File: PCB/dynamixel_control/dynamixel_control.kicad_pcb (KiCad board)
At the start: 4 copper layers, 36 x 56 mm, 56 parts, among them J1 12V, J11 Dynamixel TTL, J12 Dynamixel TTL, J2 RS232, J3 5V, J4 3.3V, J5 I2C, J8 Dynamixel TTL, Q1 SSM3J372R, Q2 IPD068P03L3GATMA1, Q3 T2N7002AK, SW1 LIMIT_SWITCH, U1 R-78E5.0-0.5, U2 SN74AHC1G14, U3 LM810M3-4.63, U4 Teensy_4.0, U5 MAX3221E, U6 ICM-40627, U7 SN74LV1T34, U8 SN74LVC2G241

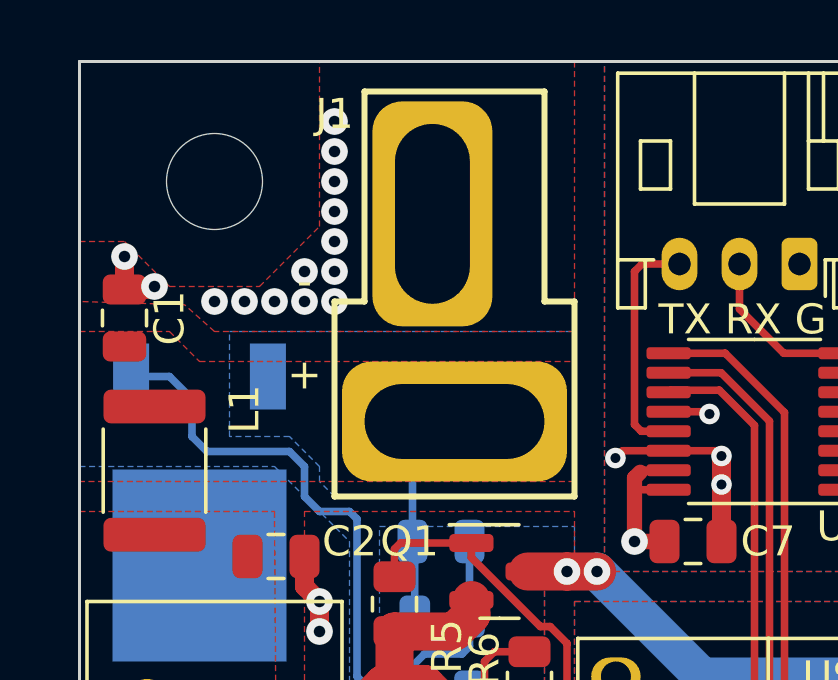
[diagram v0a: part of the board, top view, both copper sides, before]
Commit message: Fix T-Connector
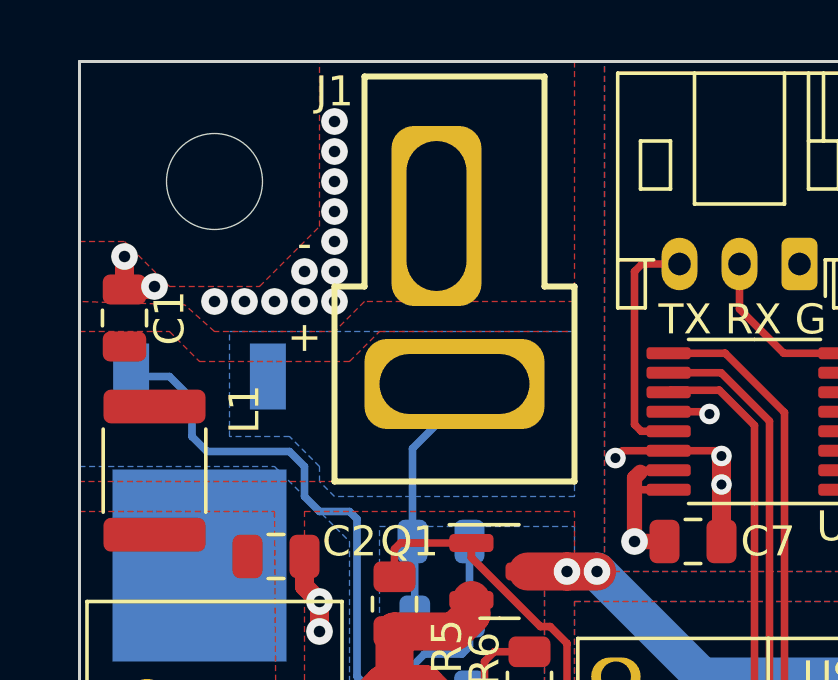
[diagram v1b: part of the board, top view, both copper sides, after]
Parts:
- moved J1 1.25 mm to (32.5, 30.8)
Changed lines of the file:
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@@
   )
   (footprint "t-top:t-connector" (layer "F.Cu")
-    (at 32.5 32 180)
+    (at 32.5 30.75 180)
     (property "Sheetfile" "dynamixel_control.kicad_sch")
     (property "Sheetname" "")
     (attr through_hole)
-    (fp_text reference "J1" (at 4 10.25 unlocked) (layer "F.SilkS")
+    (fp_text reference "J1" (at 4 9.75 unlocked) (layer "F.SilkS")
       (effects (font (size 1 1) (thickness 0.15)))
     )
@@
       (effects (font (size 1 1) (thickness 0.15)))
     )
-    (fp_line (start 3 11) (end 3 4) (layer "F.SilkS") (width 0.2))
-    (fp_line (start 3 4) (end 4 4) (layer "F.SilkS") (width 0.2))
-    (fp_line (start -3 11) (end 3 11) (layer "F.SilkS") (width 0.2))
-    (fp_line (start -4 4) (end -3 4) (layer "F.SilkS") (width 0.2))
-    (fp_line (start 4 -2.5) (end -4 -2.5) (layer "F.SilkS") (width 0.2))
-    (fp_line (start -3 4) (end -3 11) (layer "F.SilkS") (width 0.2))
-    (fp_line (start 4 4) (end 4 -2.5) (layer "F.SilkS") (width 0.2))
-    (fp_line (start -4 -2.5) (end -4 4) (layer "F.SilkS") (width 0.2))
-    (fp_line (start 4.5 -3) (end 4.5 11.5) (layer "F.CrtYd") (width 0.05))
-    (fp_line (start 4.5 11.5) (end -4.5 11.5) (layer "F.CrtYd") (width 0.05))
-    (fp_line (start -4.5 -3) (end 4.5 -3) (layer "F.CrtYd") (width 0.05))
-    (fp_line (start -4.5 11.5) (end -4.5 -3) (layer "F.CrtYd") (width 0.05))
-    (pad "1" thru_hole roundrect (at 0.7366 6.9215 180) (size 4 7.5) (drill oval 2.5 6) (layers *.Cu *.Mask) (roundrect_rratio 0.25)
+    (fp_line (start -4 -3.25) (end -4 3.25) (layer "F.SilkS") (width 0.2))
+    (fp_line (start 3 10.25) (end 3 3.25) (layer "F.SilkS") (width 0.2))
+    (fp_line (start 3 3.25) (end 4 3.25) (layer "F.SilkS") (width 0.2))
+    (fp_line (start -4 3.25) (end -3 3.25) (layer "F.SilkS") (width 0.2))
+    (fp_line (start -3 3.25) (end -3 10.25) (layer "F.SilkS") (width 0.2))
+    (fp_line (start -3 10.25) (end 3 10.25) (layer "F.SilkS") (width 0.2))
+    (fp_line (start 4 -3.25) (end -4 -3.25) (layer "F.SilkS") (width 0.2))
+    (fp_line (start 4 3.25) (end 4 -3.25) (layer "F.SilkS") (width 0.2))
+    (fp_line (start -4.5 10.75) (end -4.5 -3.75) (layer "F.CrtYd") (width 0.05))
+    (fp_line (start 4.5 -3.75) (end 4.5 10.75) (layer "F.CrtYd") (width 0.05))
+    (fp_line (start -4.5 -3.75) (end 4.5 -3.75) (layer "F.CrtYd") (width 0.05))
+    (fp_line (start 4.5 10.75) (end -4.5 10.75) (layer "F.CrtYd") (width 0.05))
+    (pad "1" thru_hole roundrect (at 0.6 5.6 180) (size 3 6) (drill oval 2 5) (layers *.Cu *.Mask) (roundrect_rratio 0.25)
       (net 2 "GND") (pinfunction "Pin_1") (pintype "passive"))
-    (pad "2" thru_hole roundrect (at 0 0 270) (size 4 7.5) (drill oval 2.5 6) (layers *.Cu *.Mask) (roundrect_rratio 0.25)
+    (pad "2" thru_hole roundrect (at 0 0 270) (size 3 6) (drill oval 2 5) (layers *.Cu *.Mask) (roundrect_rratio 0.25)
       (net 1 "+12V") (pinfunction "Pin_2") (pintype "passive"))
   )
@@
     (polygon
       (pts
-        (xy 36.5 29)
+        (xy 36.5 28)
+        (xy 29.5 28)
+        (xy 28.5 29)
         (xy 24.5 29)
         (xy 23.5 28.105963)
@@
         (xy 23 29)
         (xy 24 30)
-        (xy 36.5 30)
+        (xy 29 30)
+        (xy 30 29)
+        (xy 36.5 29)
       )
     )

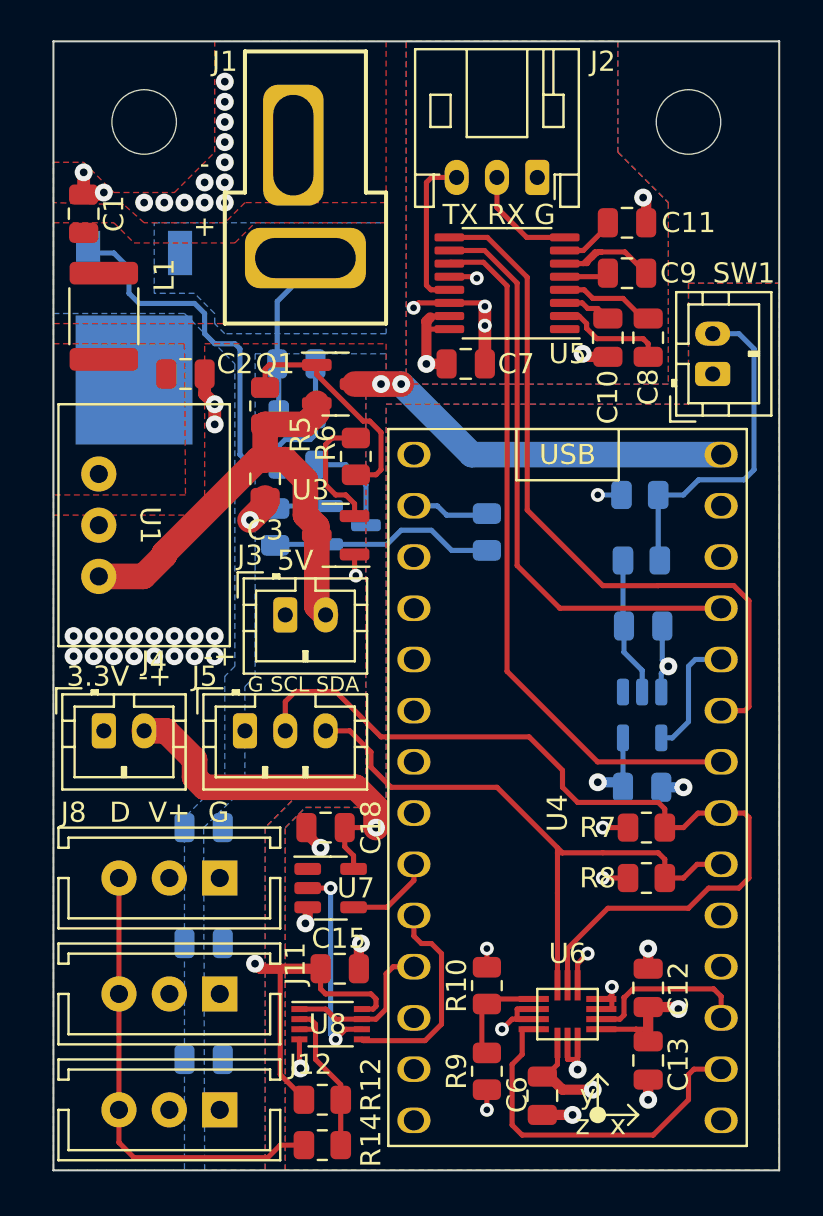
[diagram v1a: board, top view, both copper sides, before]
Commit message: Add Debug UART connector to dynamixel_control.
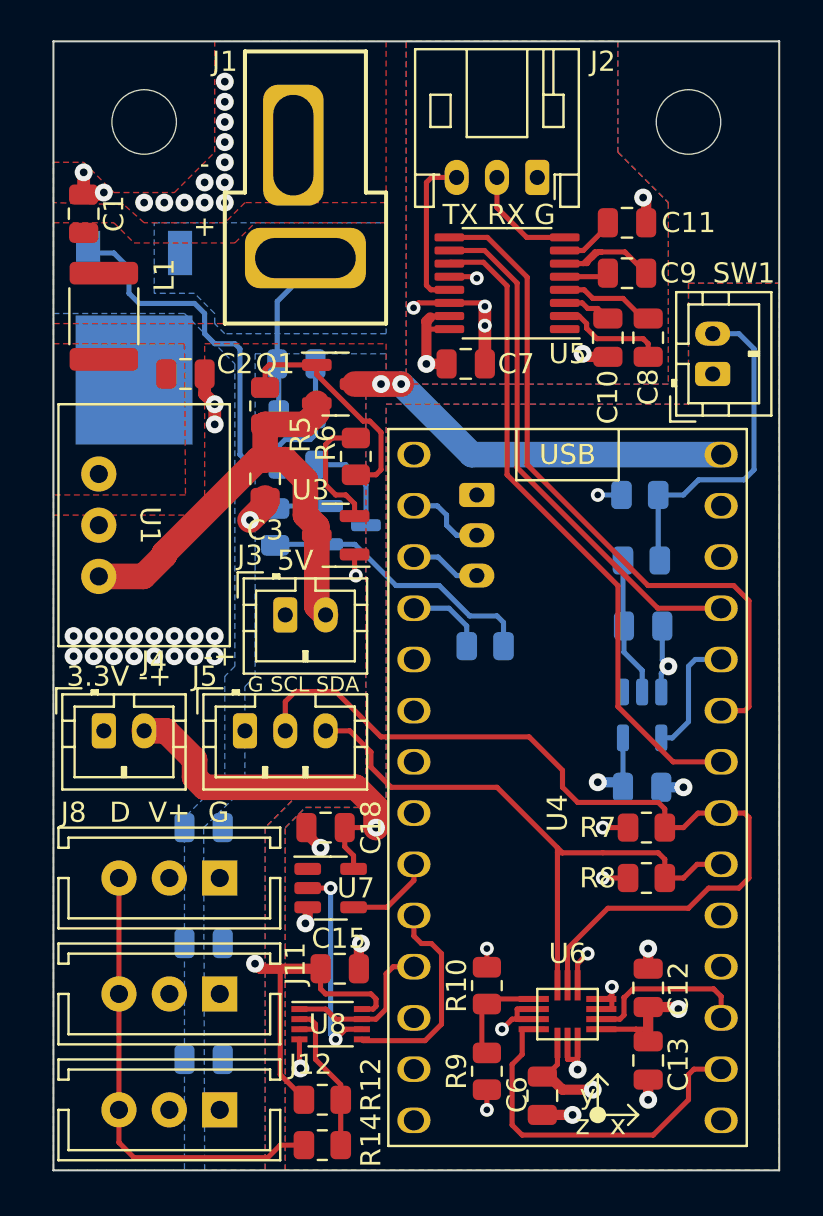
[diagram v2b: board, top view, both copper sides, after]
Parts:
- added J6: Debug Uart, Connector_JST:JST_PH_B3B-PH-K_1x03_P2.00mm_Vertical, B.Cu at (41.0, 42.5)
- moved R17 5.66 mm to (41.4, 50.0), turned to 0 degrees
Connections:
- U4 pad 0: /Dynamixel/DYNAMIXEL_ENABLE -> /DEBUG_UART_RX
- U4 pad 1: unconnected-(U4-Pad1) -> /DEBUG_UART_TX
- U4 pad 2: unconnected-(U4-Pad2) -> /Dynamixel/DYNAMIXEL_ENABLE
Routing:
- net /DEBUG_UART_RX: track 0.00 -> 4.02 mm
- net /DEBUG_UART_TX: track 0.00 -> 3.50 mm
- net Net-(Q3-Pad1): track 11.2 -> 14.1 mm
- net /~{RS232_INVALID}: track 29.0 -> 26.2 mm
- net /UART_TX: track 35.0 -> 32.8 mm
- net /UART_RX: track 35.8 -> 34.5 mm
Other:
- board text added: "Debug"
- board text added: "G RX TX"
